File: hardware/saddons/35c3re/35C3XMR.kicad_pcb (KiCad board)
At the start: 2 copper layers, 100 x 95 mm, 92 parts, among them U1 TLC555, U2 74HCT04, X1 Shitty_conn

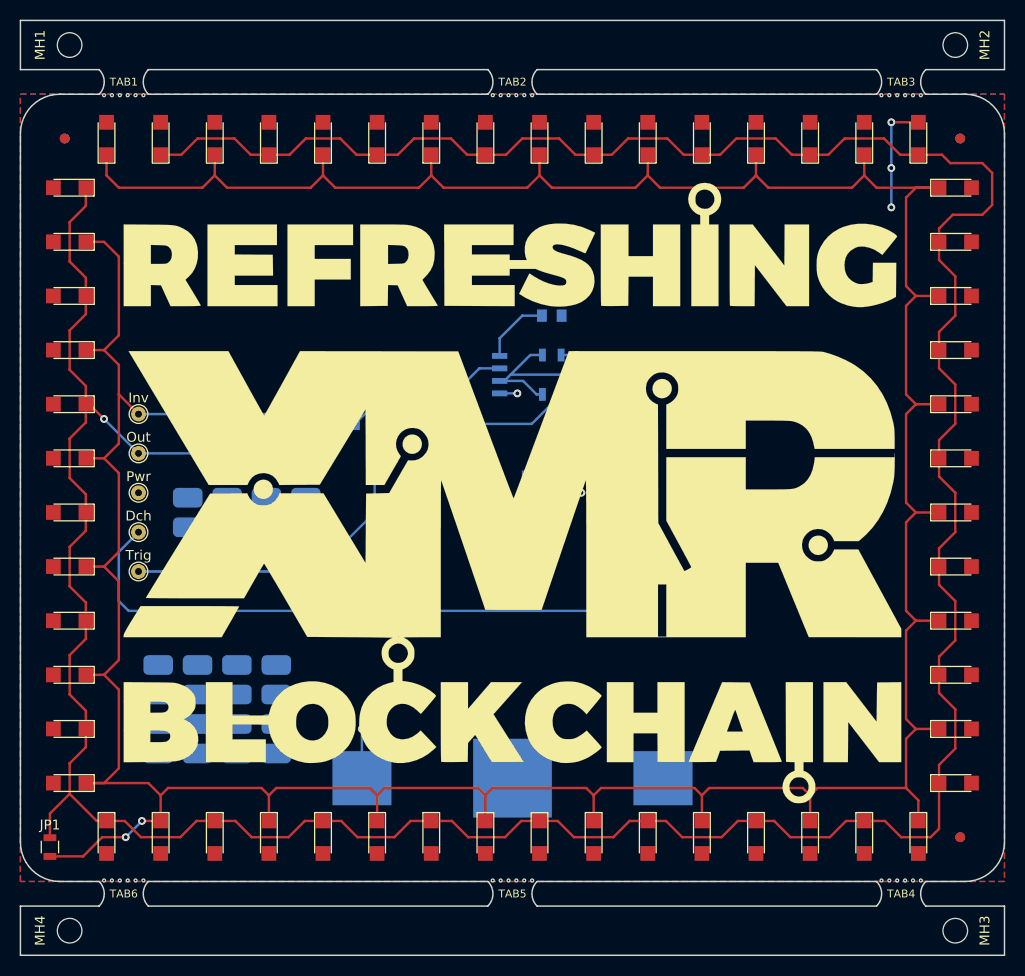
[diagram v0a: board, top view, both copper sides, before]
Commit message: Corrected and improved design to beta grade quality pending release; Added second battery, added Monero graphics, removed third party logos, corrected inverter circuit, corrected weak pin fastener, corrected astable values, added bill of materials, added manufacturing guides, added worksheet templates, corrected stencil mounts, enlarged mousebites, improved fiducial marks, and corrected inverter symbol.
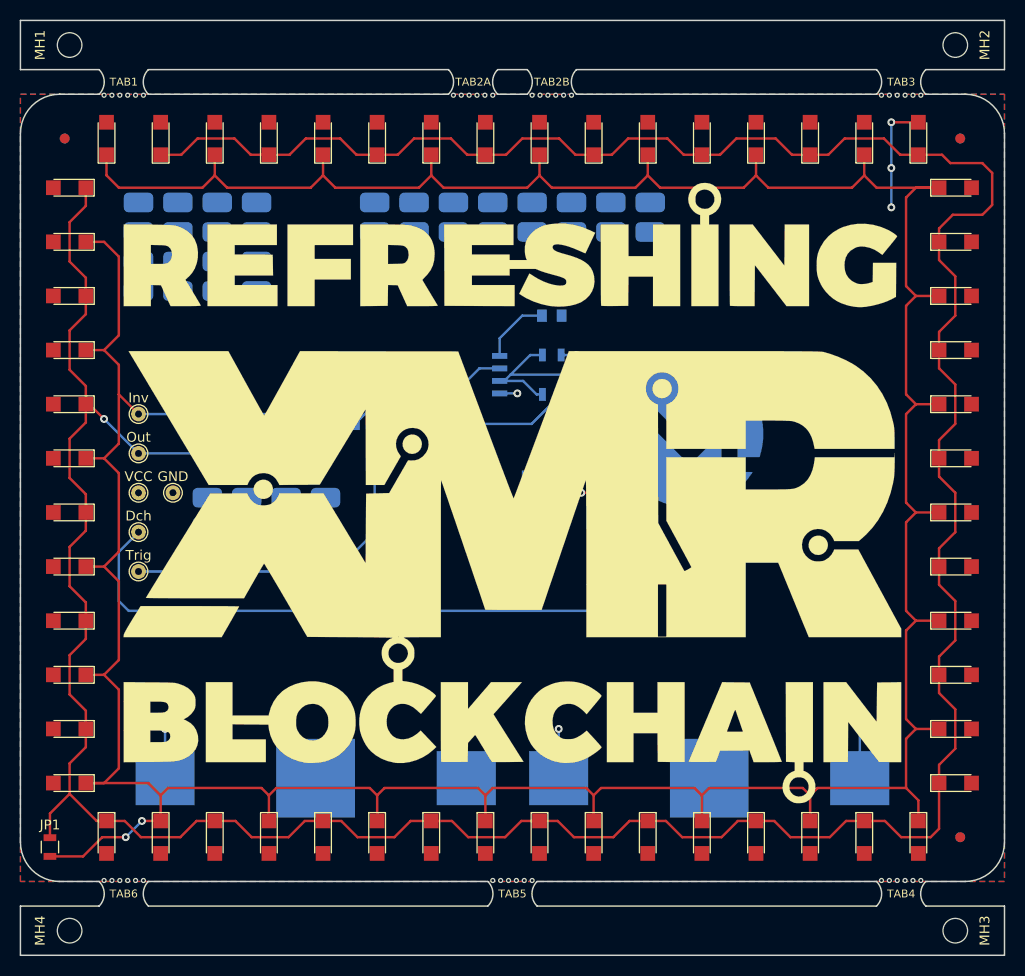
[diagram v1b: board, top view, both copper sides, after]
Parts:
- removed BT1: Battery_Cell, Monero_Local:BatteryHolder_Keystone_3008_1x2450
- removed the G1 at (117.0, 80.0)
- added CR2450-A: Battery_Cell, Monero_Local:BatteryHolder_Keystone_3008_1x2450, B.Cu at (110.0, 117.0)
- added CR2450-B: Battery_Cell, Monero_Local:BatteryHolder_Keystone_3008_1x2450, B.Cu at (70.0, 117.0)
- added GND: TEST, Monero_Local:TestPoint_THTPad_D1.5mm_Drill0.7mm, F.Cu at (55.5, 88.0)
- added LOGO2: Moneroball, Monero_Local:Moneroball_15mm, B.Cu at (108.0, 82.0)
- added SF4: Soldfeld, Monero_Local:Solderarea, B.Cu at (82.0, 60.0)
- added SF5: Soldfeld, Monero_Local:Solderarea, B.Cu at (98.0, 60.0)
- added TAB2B: Panel_Mousetab_25mm_Single, Monero_Local:Panel_Mousetab_25mm_Single, F.Cu at (94.0, 46.2)
- C1: value 47uF -> 4,7uF
- FID1, FID3, FID5: value Dummy_FIDUCIAL_Passermarke_Type1_RevE_Date16Nov2011 -> FiducialPassermarke-Top; footprint Monero_Local:Fiducial_1mm_Dia_2.54mm_Outer_CopperTop -> Monero_Local:Fiducial_1mm_Dia_2.54mm
- FID2, FID4, FID6: value Dummy_FIDUCIAL_Passermarke_Type1_RevE_Date16Nov2011 -> FiducialPassermarke-Bot; footprint Monero_Local:Fiducial_1mm_Dia_2.54mm_Outer_CopperBottom -> Monero_Local:Fiducial_1mm_Dia_2.54mm; moved to B.Cu
- R2: value 47.5K -> 100K
- U2: value 74HCT04 -> NC7SZ04L6X
- moved FID2 115.4 mm to (44.5, 52.0)
- moved FID6 115.4 mm to (135.5, 123.0)
- moved FID3 71.0 mm to (135.5, 52.0)
- moved FID5 71.0 mm to (135.5, 123.0)
- moved SF2 47.0 mm to (58.0, 60.0)
- moved SF3 47.0 mm to (58.0, 66.0)
- moved G1 33.0 mm to (126.5, 82.0)
- moved TAB2A 4.00 mm to (86.0, 46.2)
- moved SF1 2.00 mm to (65.0, 90.0)
- moved U2 1.18 mm to (75.4, 75.0), turned to 90 degrees
- renumbered G2 to G1, LOGOFUN1 to LOGO1, X1 to SAO1, TAB2 to TAB2A, Pwr to VCC
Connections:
- U2 pad 1: Net-(D10-Pad1) -> (no net)
- U2 pad 2: Net-(D1-Pad1) -> Net-(D10-Pad1)
- U2 pad 3: (no net) -> GND
- U2 pad 4: (no net) -> Net-(D1-Pad1)
- U2 pad 6: (no net) -> +3V3
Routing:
- net +3V3: track 30.0 -> 45.9 mm, vias 9 -> 11
- net GND: track 14.6 -> 19.0 mm
- net Net-(C1-Pad1): track 69.2 -> 70.4 mm
- net Net-(D10-Pad1): track 390.7 -> 391.5 mm
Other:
- outline, holes or cut-outs redrawn
- board text added: "<- Stencil8"
- board text added: "Copyright © 2018, The Monero Project CERN Open Hardware Licence 1.2 Astable CMOS Timer Badge 0.8.4"
- board text added: "Dch"
- board text added: "Epoxy or solder fastener"
- board text added: "GND"
- board text added: "Hack these solderfields"
- board text added: "Inv"
- board text added: "Manufacturing automation rail edge to be optionally removed"
- board text added: "Nothing here, please look away..."
- board text added: "Out"
- board text added: "Please fully drill the four mount holes (MH) through the stencil!"
- board text added: "Stencil8 ->"
- board text added: "Trig"
- board text added: "VCC"
- board text removed: "Copyright © 2018, The Monero Project CERN Open Hardware Licence 1.2 Limited edition Monero badges Hardware revision 0.8.3"

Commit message: Documented unconnected parts to reduce unintentional short circuits.
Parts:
- renumbered JP1 to NC
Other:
- board text added: "Copyright © 2018, The Monero Project CERN Open Hardware Licence 1.2 Astable CMOS Timer Badge 0.8.5"
- board text removed: "Copyright © 2018, The Monero Project CERN Open Hardware Licence 1.2 Astable CMOS Timer Badge 0.8.4"
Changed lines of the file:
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@@
     (title "AStable Timer LED Badge")
     (date 2018-12-31)
-    (rev 0.8.4)
+    (rev 0.8.5)
     (company "The Monero Project, Hardware Team")
     (comment 1 "Copyright © 2018, The Monero Project")
-    (comment 2 "Releasing a protograde congress edition")
+    (comment 2 "Releasing a betagrade test edition")
     (comment 3 "Pending quality assurance testing")
     (comment 4 "Warning, untested prototype!")
@@
     (tags "resistor 0805")
     (attr smd)
-    (fp_text reference JP1 (at -2.25 0) (layer F.SilkS)
+    (fp_text reference NC (at -2.25 0) (layer F.SilkS)
       (effects (font (size 1 1) (thickness 0.15)))
     )
@@
     (effects (font (size 1.5 1.5) (thickness 0.3)) (justify left))
   )
-  (gr_text "Copyright © 2018, The Monero Project\nCERN Open Hardware Licence 1.2\nAstable CMOS Timer Badge 0.8.4" (at 134 96) (layer B.SilkS)
+  (gr_text "Copyright © 2018, The Monero Project\nCERN Open Hardware Licence 1.2\nAstable CMOS Timer Badge 0.8.5" (at 134 96) (layer B.SilkS)
     (effects (font (size 1.5 1.5) (thickness 0.3)) (justify left mirror))
   )
